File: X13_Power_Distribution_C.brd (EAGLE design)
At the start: 152.4 x 73.7 mm, 42 parts, among them Q1 IRF1018EPBF, Q2 SSM3K341R, Q3 IRF1018EPBF, Q4 IRF1018EPBF, Q5 SSM3K341R, Q6 SSM3K341R

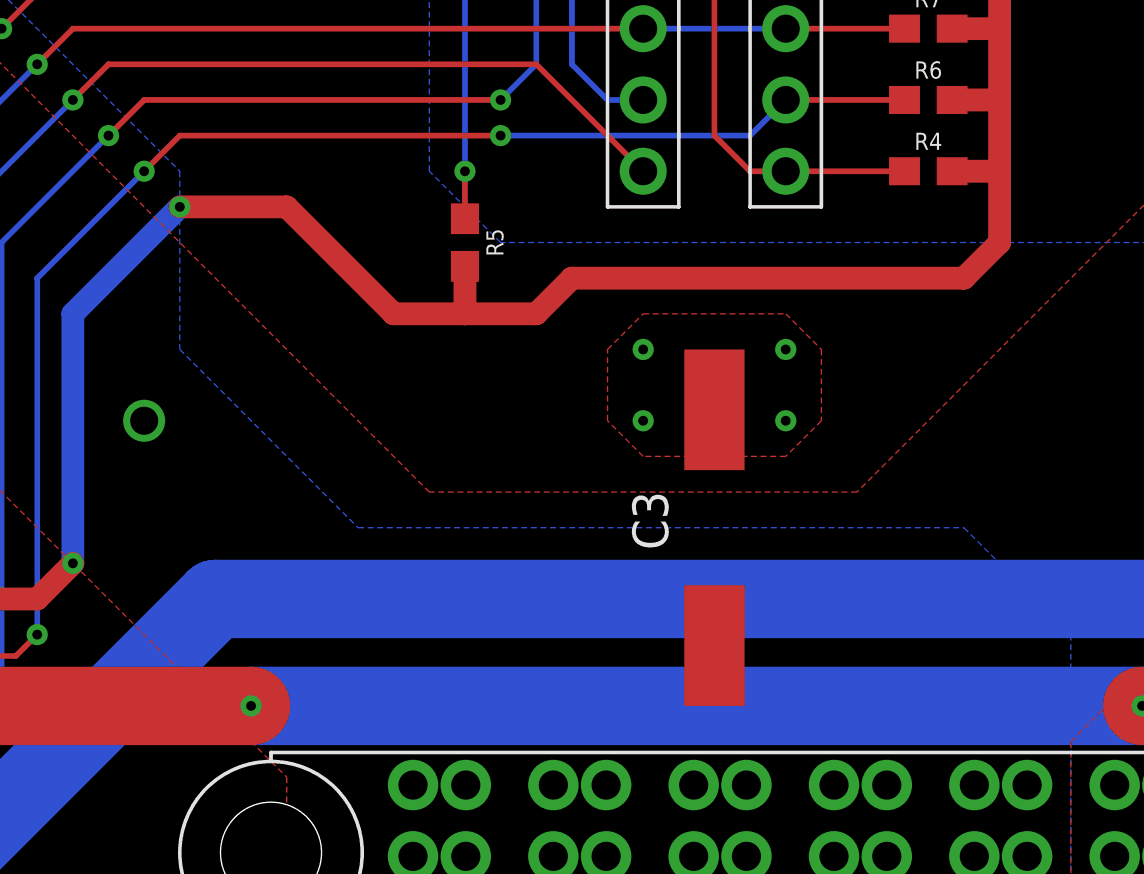
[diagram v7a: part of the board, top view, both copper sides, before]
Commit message: Moved capacitor over a bit more
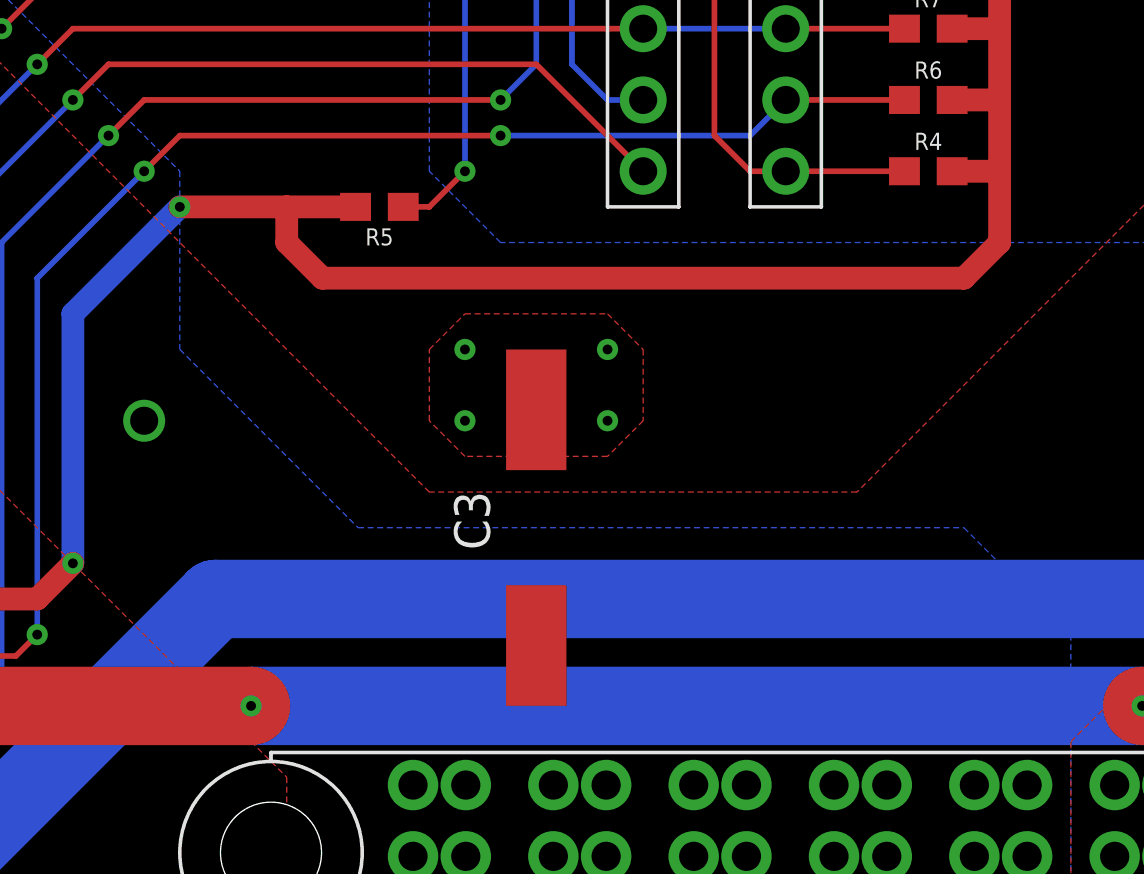
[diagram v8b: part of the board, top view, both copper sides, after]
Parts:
- moved C3 6.35 mm to (69.8, 16.5)
- moved R5 3.30 mm to (64.3, 27.9), turned to 180 degrees
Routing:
- net ALERT_1: track 71.9 -> 73.0 mm
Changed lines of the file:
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@@
 <attribute name="VALUE" x="116.84" y="36.322" size="0.6096" layer="28" font="vector" ratio="20" rot="MR180" align="top-center"/>
 </element>
-<element name="C3" library="brick-capacitor-UCM1H331MNL1GS" package="CAPAE1030X1050N" package3d_urn="urn:adsk.eagle:package:24202090/2" value="330uF" x="76.2" y="16.51" smashed="yes" rot="R90">
-<attribute name="ARROW_PART_NUMBER" value="UCM1H331MNL1GS" x="76.2" y="16.51" size="1.778" layer="27" rot="R90" display="off"/>
-<attribute name="ARROW_PRICE-STOCK" value="https://www.arrow.com/en/products/ucm1h331mnl1gs/nichicon" x="76.2" y="16.51" size="1.778" layer="27" rot="R90" display="off"/>
-<attribute name="DESCRIPTION" value="Nichicon 330uF 50 V Aluminium Electrolytic Capacitor SMD, CM Series 2000h 10 (Dia.) x 10mm" x="76.2" y="16.51" size="1.778" layer="27" rot="R90" display="off"/>
-<attribute name="HEIGHT" value="10.5mm" x="76.2" y="16.51" size="1.778" layer="27" rot="R90" display="off"/>
-<attribute name="MANUFACTURER_NAME" value="Nichicon" x="76.2" y="16.51" size="1.778" layer="27" rot="R90" display="off"/>
-<attribute name="MANUFACTURER_PART_NUMBER" value="UCM1H331MNL1GS" x="76.2" y="16.51" size="1.778" layer="27" rot="R90" display="off"/>
-<attribute name="MOUSER_PART_NUMBER" value="647-UCM1H331MNL1GS" x="76.2" y="16.51" size="1.778" layer="27" rot="R90" display="off"/>
-<attribute name="MOUSER_PRICE-STOCK" value="https://www.mouser.co.uk/ProductDetail/Nichicon/UCM1H331MNL1GS?qs=DSgADHjnLTkTovFLdbC%252BNg%3D%3D" x="76.2" y="16.51" size="1.778" layer="27" rot="R90" display="off"/>
-<attribute name="NAME" x="73.914" y="16.764" size="1.27" layer="25" rot="R90" align="center"/>
-<attribute name="VALUE" x="78.74" y="16.51" size="1.27" layer="27" rot="R90" align="center"/>
+<element name="C3" library="brick-capacitor-UCM1H331MNL1GS" package="CAPAE1030X1050N" package3d_urn="urn:adsk.eagle:package:24202090/2" value="330uF" x="69.85" y="16.51" smashed="yes" rot="R90">
+<attribute name="ARROW_PART_NUMBER" value="UCM1H331MNL1GS" x="69.85" y="16.51" size="1.778" layer="27" rot="R90" display="off"/>
+<attribute name="ARROW_PRICE-STOCK" value="https://www.arrow.com/en/products/ucm1h331mnl1gs/nichicon" x="69.85" y="16.51" size="1.778" layer="27" rot="R90" display="off"/>
+<attribute name="DESCRIPTION" value="Nichicon 330uF 50 V Aluminium Electrolytic Capacitor SMD, CM Series 2000h 10 (Dia.) x 10mm" x="69.85" y="16.51" size="1.778" layer="27" rot="R90" display="off"/>
+<attribute name="HEIGHT" value="10.5mm" x="69.85" y="16.51" size="1.778" layer="27" rot="R90" display="off"/>
+<attribute name="MANUFACTURER_NAME" value="Nichicon" x="69.85" y="16.51" size="1.778" layer="27" rot="R90" display="off"/>
+<attribute name="MANUFACTURER_PART_NUMBER" value="UCM1H331MNL1GS" x="69.85" y="16.51" size="1.778" layer="27" rot="R90" display="off"/>
+<attribute name="MOUSER_PART_NUMBER" value="647-UCM1H331MNL1GS" x="69.85" y="16.51" size="1.778" layer="27" rot="R90" display="off"/>
+<attribute name="MOUSER_PRICE-STOCK" value="https://www.mouser.co.uk/ProductDetail/Nichicon/UCM1H331MNL1GS?qs=DSgADHjnLTkTovFLdbC%252BNg%3D%3D" x="69.85" y="16.51" size="1.778" layer="27" rot="R90" display="off"/>
+<attribute name="NAME" x="67.564" y="16.764" size="1.27" layer="25" rot="R90" align="center"/>
+<attribute name="VALUE" x="72.39" y="16.51" size="1.27" layer="27" rot="R90" align="center"/>
 </element>
 <element name="5V_POE" library="Dist_POE" package="CONN2_282834-2_TEC" value="POE_TERMINAL" x="127" y="10.16" smashed="yes" rot="R180">
@@
 </element>
 <element name="BACKPLANE_LOGIC" library="Backplane_Dist_Logic_Connector" package="IPL1-107-01-L-D-RE-P" value="IPL1-107-01-L-D-RE-P" x="25.4" y="11.43" smashed="yes"/>
-<element name="R5" library="SparkFun-Resistors" library_urn="urn:adsk.eagle:library:532" package="0603" package3d_urn="urn:adsk.eagle:package:39650/1" value="10k" x="67.31" y="26.67" smashed="yes" rot="R270">
-<attribute name="NAME" x="68.072" y="26.67" size="0.6096" layer="25" font="vector" ratio="20" rot="R270" align="bottom-center"/>
-<attribute name="PROD_ID" value=" " x="67.31" y="26.67" size="1.016" layer="27" rot="R270" display="off"/>
-<attribute name="VALUE" x="66.548" y="26.67" size="0.6096" layer="27" font="vector" ratio="20" rot="R270" align="top-center"/>
+<element name="R5" library="SparkFun-Resistors" library_urn="urn:adsk.eagle:library:532" package="0603" package3d_urn="urn:adsk.eagle:package:39650/1" value="10k" x="64.262" y="27.94" smashed="yes" rot="R180">
+<attribute name="NAME" x="64.262" y="27.178" size="0.6096" layer="25" font="vector" ratio="20" rot="R180" align="bottom-center"/>
+<attribute name="PROD_ID" value=" " x="64.262" y="27.94" size="1.016" layer="27" rot="R180" display="off"/>
+<attribute name="VALUE" x="64.262" y="28.702" size="0.6096" layer="27" font="vector" ratio="20" rot="R180" align="top-center"/>
 </element>
 <element name="BACKPLANE_PWR" library="Samtec MPPT Hermaphoditic 10 pos - MPPT-10-01-01-L-RA-SD" package="MPPT-10-01-01-L-RA-SD" package3d_urn="urn:adsk.eagle:package:25115828/2" value="" x="88.9" y="0" smashed="yes"/>
@@
 <wire x1="133.35" y1="24.13" x2="128.27" y2="24.13" width="0.2032" layer="1"/>
 <polygon width="0.8128" layer="1">
-<vertex x="72.39" y="22.86"/>
-<vertex x="73.66" y="24.13"/>
-<vertex x="78.74" y="24.13"/>
-<vertex x="80.01" y="22.86"/>
-<vertex x="80.01" y="20.32"/>
-<vertex x="78.74" y="19.05"/>
-<vertex x="73.66" y="19.05"/>
-<vertex x="72.39" y="20.32"/>
-</polygon>
-<via x="73.66" y="22.86" extent="1-16" drill="0.35"/>
-<via x="73.66" y="20.32" extent="1-16" drill="0.35"/>
-<via x="78.74" y="20.32" extent="1-16" drill="0.35"/>
-<via x="78.74" y="22.86" extent="1-16" drill="0.35"/>
+<vertex x="66.04" y="22.86"/>
+<vertex x="67.31" y="24.13"/>
+<vertex x="72.39" y="24.13"/>
+<vertex x="73.66" y="22.86"/>
+<vertex x="73.66" y="20.32"/>
+<vertex x="72.39" y="19.05"/>
+<vertex x="67.31" y="19.05"/>
+<vertex x="66.04" y="20.32"/>
+</polygon>
+<via x="67.31" y="22.86" extent="1-16" drill="0.35"/>
+<via x="67.31" y="20.32" extent="1-16" drill="0.35"/>
+<via x="72.39" y="20.32" extent="1-16" drill="0.35"/>
+<via x="72.39" y="22.86" extent="1-16" drill="0.35"/>
 </signal>
 <signal name="+3.3V">
@@
 <contactref element="CONVERSION" pad="4"/>
 <via x="57.15" y="27.94" extent="1-16" drill="0.35"/>
-<wire x1="60.96" y1="27.94" x2="57.15" y2="27.94" width="0.8128" layer="1"/>
+<wire x1="57.15" y1="27.94" x2="60.96" y2="27.94" width="0.8128" layer="1"/>
 <wire x1="53.34" y1="24.13" x2="57.15" y2="27.94" width="0.8128" layer="16"/>
 <wire x1="34.29" y1="13.97" x2="44.45" y2="13.97" width="0.8128" layer="16"/>
@@
 <wire x1="84.67" y1="29.21" x2="86.36" y2="29.21" width="0.8128" layer="1"/>
 <wire x1="86.36" y1="29.21" x2="86.36" y2="31.75" width="0.8128" layer="1"/>
-<wire x1="67.31" y1="25.82" x2="67.31" y2="24.13" width="0.8128" layer="1"/>
-<wire x1="67.31" y1="24.13" x2="64.77" y2="24.13" width="0.8128" layer="1"/>
-<wire x1="64.77" y1="24.13" x2="60.96" y2="27.94" width="0.8128" layer="1"/>
-<wire x1="67.31" y1="24.13" x2="69.85" y2="24.13" width="0.8128" layer="1"/>
-<wire x1="69.85" y1="24.13" x2="71.12" y2="25.4" width="0.8128" layer="1"/>
-<wire x1="71.12" y1="25.4" x2="85.09" y2="25.4" width="0.8128" layer="1"/>
+<wire x1="62.23" y1="25.4" x2="85.09" y2="25.4" width="0.8128" layer="1"/>
 <wire x1="85.09" y1="25.4" x2="86.36" y2="26.67" width="0.8128" layer="1"/>
 <wire x1="86.36" y1="26.67" x2="86.36" y2="29.21" width="0.8128" layer="1"/>
@@
 <wire x1="106.68" y1="46.99" x2="101.6" y2="52.07" width="0.8128" layer="1"/>
 <wire x1="101.6" y1="52.07" x2="95.25" y2="52.07" width="0.8128" layer="1"/>
+<wire x1="60.96" y1="27.94" x2="63.412" y2="27.94" width="0.8128" layer="1"/>
+<wire x1="62.23" y1="25.4" x2="60.96" y2="26.67" width="0.8128" layer="1"/>
+<wire x1="60.96" y1="26.67" x2="60.96" y2="27.94" width="0.8128" layer="1"/>
 </signal>
 <signal name="C2_2">
@@
 <wire x1="53.34" y1="36.83" x2="67.31" y2="36.83" width="0.2032" layer="1"/>
 <wire x1="67.31" y1="36.83" x2="73.66" y2="36.83" width="0.2032" layer="1"/>
-<wire x1="67.31" y1="27.52" x2="67.31" y2="29.21" width="0.2032" layer="1"/>
+<wire x1="65.112" y1="27.94" x2="66.04" y2="27.94" width="0.2032" layer="1"/>
+<wire x1="66.04" y1="27.94" x2="67.31" y2="29.21" width="0.2032" layer="1"/>
 <via x="67.31" y="29.21" extent="1-16" drill="0.35"/>
 <wire x1="67.31" y1="29.21" x2="67.31" y2="36.83" width="0.2032" layer="16"/>
